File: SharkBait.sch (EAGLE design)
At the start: 12 parts

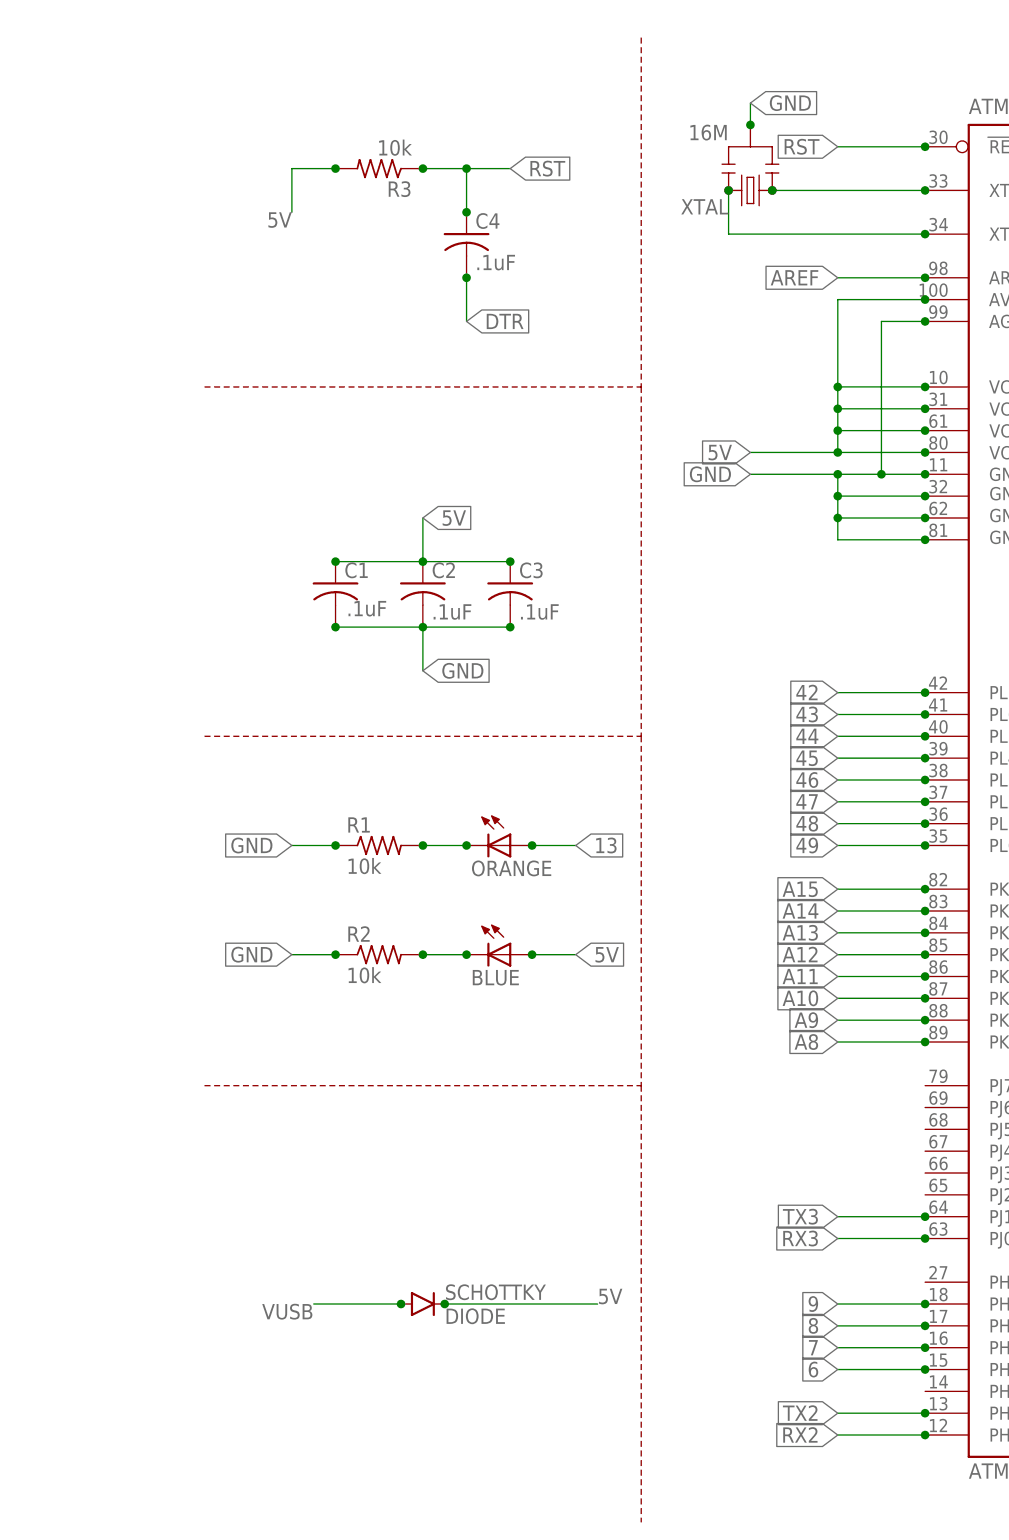
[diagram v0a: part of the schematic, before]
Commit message: menambahkan pin uploader
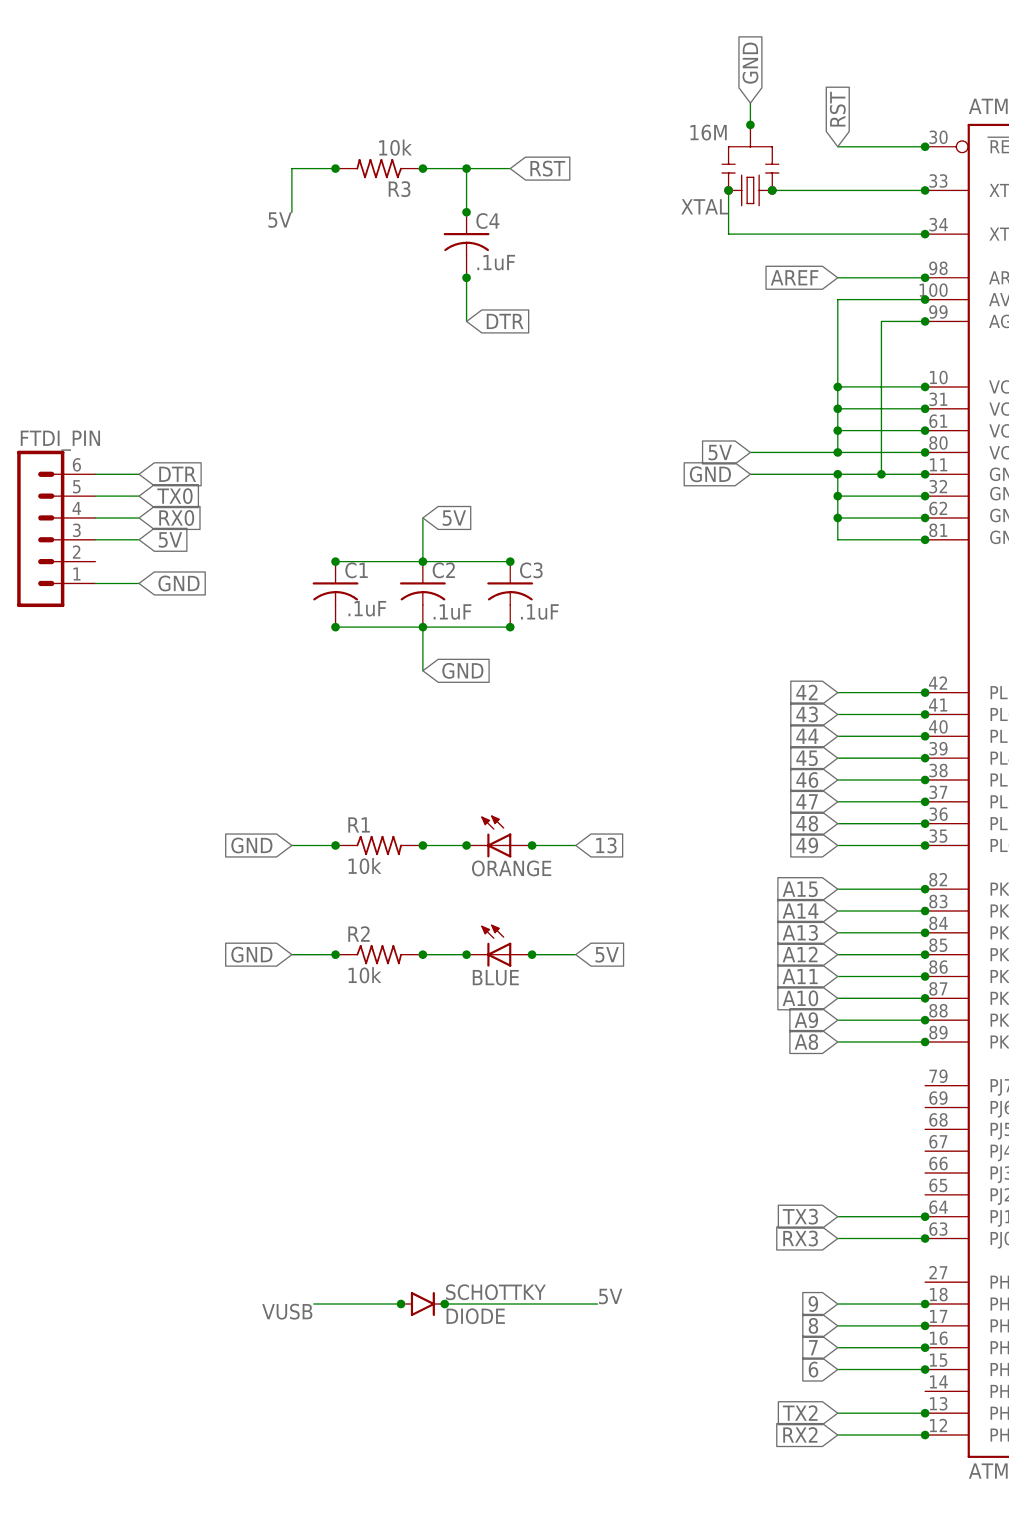
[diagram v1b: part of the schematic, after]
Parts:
- added FTDI_PIN: (no value), con-lstb:MA06-1
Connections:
- net 5V: now also FTDI_PIN.3
- net DTR: now also FTDI_PIN.6
- net GND: now also FTDI_PIN.1
- net RX0: now also FTDI_PIN.4
- net TX0: now also FTDI_PIN.5
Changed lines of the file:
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@@
 <part name="C4" library="Fuzzy" deviceset="CAPACITOR-SMD-0805" device="" value=".1uF"/>
 <part name="SCHOTTKY" library="Fuzzy" deviceset="DIODE" device="" value="DIODE"/>
+<part name="FTDI_PIN" library="con-lstb" deviceset="MA06-1" device=""/>
 </parts>
 <sheets>
 <sheet>
 <plain>
-<wire x1="-99.06" y1="162.56" x2="-99.06" y2="121.92" width="0.1" layer="94" style="longdash"/>
-<wire x1="-99.06" y1="121.92" x2="-99.06" y2="81.28" width="0.1" layer="94" style="longdash"/>
-<wire x1="-99.06" y1="81.28" x2="-99.06" y2="40.64" width="0.1" layer="94" style="longdash"/>
-<wire x1="-99.06" y1="40.64" x2="-99.06" y2="-10.16" width="0.1" layer="94" style="longdash"/>
-<wire x1="-149.86" y1="121.92" x2="-99.06" y2="121.92" width="0.1" layer="94" style="longdash"/>
-<wire x1="-149.86" y1="81.28" x2="-99.06" y2="81.28" width="0.1" layer="94" style="longdash"/>
-<wire x1="-149.86" y1="40.64" x2="-99.06" y2="40.64" width="0.1" layer="94" style="longdash"/>
 <text x="-137.16" y="76.2" size="2" layer="98" ratio="15">Indicator LED's</text>
 <text x="-137.16" y="116.84" size="2" layer="98" ratio="15">Bypass Capacitors</text>
@@
 <instance part="C4" gate="G$1" x="-119.38" y="139.7"/>
 <instance part="SCHOTTKY" gate="G$1" x="-124.46" y="15.24"/>
+<instance part="FTDI_PIN" gate="1" x="-170.18" y="106.68"/>
 </instances>
 <busses>
@@
 <junction x="-121.92" y="15.24"/>
 <wire x1="-121.92" y1="15.24" x2="-104.14" y2="15.24" width="0.1524" layer="91"/>
+</segment>
+<segment>
+<pinref part="FTDI_PIN" gate="1" pin="3"/>
+<wire x1="-162.56" y1="104.14" x2="-157.48" y2="104.14" width="0.1524" layer="91"/>
+<label x="-157.48" y="104.14" size="1.778" layer="95" xref="yes"/>
 </segment>
 </net>
@@
 <pinref part="XTAL" gate="G$1" pin="2"/>
 <wire x1="-86.36" y1="152.4" x2="-86.36" y2="154.94" width="0.1524" layer="91"/>
-<label x="-86.36" y="154.94" size="1.778" layer="95" xref="yes"/>
+<label x="-86.36" y="154.94" size="1.778" layer="95" rot="R90" xref="yes"/>
 <junction x="-86.36" y="152.4"/>
 </segment>
@@
 <junction x="-134.62" y="55.88"/>
 </segment>
+<segment>
+<pinref part="FTDI_PIN" gate="1" pin="1"/>
+<wire x1="-162.56" y1="99.06" x2="-157.48" y2="99.06" width="0.1524" layer="91"/>
+<label x="-157.48" y="99.06" size="1.778" layer="95" xref="yes"/>
+</segment>
 </net>
 <net name="RST" class="0">
@@
 <pinref part="ATMEGA2560" gate="G$1" pin="RESET"/>
 <wire x1="-66.04" y1="149.86" x2="-76.2" y2="149.86" width="0.1524" layer="91"/>
-<label x="-76.2" y="149.86" size="1.778" layer="95" rot="R180" xref="yes"/>
+<label x="-76.2" y="149.86" size="1.778" layer="95" rot="R90" xref="yes"/>
 <junction x="-66.04" y="149.86"/>
 </segment>
@@
 <junction x="-119.38" y="134.62"/>
 </segment>
+<segment>
+<pinref part="FTDI_PIN" gate="1" pin="6"/>
+<wire x1="-162.56" y1="111.76" x2="-157.48" y2="111.76" width="0.1524" layer="91"/>
+<label x="-157.48" y="111.76" size="1.778" layer="95" xref="yes"/>
+</segment>
 </net>
 <net name="N$82" class="0">
@@
 <junction x="5.08" y="40.64"/>
 </segment>
+<segment>
+<pinref part="FTDI_PIN" gate="1" pin="4"/>
+<wire x1="-162.56" y1="106.68" x2="-157.48" y2="106.68" width="0.1524" layer="91"/>
+<label x="-157.48" y="106.68" size="1.778" layer="95" xref="yes"/>
+</segment>
 </net>
 <net name="TX0" class="0">
@@
 <junction x="5.08" y="43.18"/>
 </segment>
-</net>
+<segment>
+<pinref part="FTDI_PIN" gate="1" pin="5"/>
+<wire x1="-162.56" y1="109.22" x2="-157.48" y2="109.22" width="0.1524" layer="91"/>
+<label x="-157.48" y="109.22" size="1.778" layer="95" xref="yes"/>
+</segment>
+</net>

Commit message: Revisi final
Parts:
- removed FTDI_PIN: (no value), con-lstb:MA06-1
- added C11: 100uF, rcl:CPOL-USD
- added C5, C7: 100 uF, rc-master-smd:C_0805
- added C6: 100nF, rcl:C-USC1206
- added C9: 10uF, Fuzzy:CAPACITOR-SMD-0805
- added HT733: HT7333, C_HT7333_SOT89:HT7333
- added J1: BC501SM-TR, C_BC501SM-TR:BC501SM-TR
- added Q1: L78M05CDT, C_L78M05CDT:L78M05CDT
- added R10, R11, R4, R8: 1K8, rc-master-smd:R_0805
- added R12, R13, R7, R9: 3K3, rc-master-smd:R_0805
- added R5, R6: (no value), rc-master-smd:R_0805
- added U$1: WEMOS_SD_D1_MINI, C_WEMOS_SD_D1_MINI:WEMOS_SD_D1_MINI
- added U$2: SIM7000, C_SIM7000:SIM7000
- added U$3: JST-PH_5-PIN_HEADER, srg:JST-PH_5-PIN_HEADER
- added U$4: JST-PH_2-PIN_HEADER, srg:JST-PH_2-PIN_HEADER
- added U$5: JST-PH_3-PIN_HEADER, srg:JST-PH_3-PIN_HEADER
- added U$6: JST-PH_4-PIN_HEADER, srg:JST-PH_4-PIN_HEADER
- added U2: DS3231M+, C_DS3231M_:DS3231M+
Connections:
- removed net 10: ATMEGA2560.(OC2A/PCINT4)PB4
- removed net 11: ATMEGA2560.(OC1A/PCINT5)PB5
- removed net 12: ATMEGA2560.(OC1B/PCINT6)PB6
- removed net 2: ATMEGA2560.(OC3B/INT4)PE4
- removed net 20: ATMEGA2560.(SDA/INT1)PD1
- removed net 21: ATMEGA2560.(SCL/INT0)PD0
- removed net 22: ATMEGA2560.(AD0)PA0
- removed net 23: ATMEGA2560.(AD1)PA1
- removed net 24: ATMEGA2560.(AD2)PA2
- removed net 25: ATMEGA2560.(AD3)PA3
- removed net 26: ATMEGA2560.(AD4)PA4
- removed net 27: ATMEGA2560.(AD5)PA5
- removed net 28: ATMEGA2560.(AD6)PA6
- removed net 29: ATMEGA2560.(AD7)PA7
- removed net 3: ATMEGA2560.(OC3C/INT5)PE5
- removed net 30: ATMEGA2560.(A15)PC7
- removed net 31: ATMEGA2560.(A14)PC6
- removed net 32: ATMEGA2560.(A13)PC5
- removed net 33: ATMEGA2560.(A12)PC4
- removed net 34: ATMEGA2560.(A11)PC3
- removed net 35: ATMEGA2560.(A10)PC2
- removed net 36: ATMEGA2560.(A9)PC1
- removed net 37: ATMEGA2560.(A8)PC0
- removed net 38: ATMEGA2560.(T0)PD7
- removed net 39: ATMEGA2560.(ALE)PG2
- removed net 4: ATMEGA2560.(OC0B)PG5
- removed net 40: ATMEGA2560.(RD)PG1
- removed net 41: ATMEGA2560.(WR)PG0
- removed net 42: ATMEGA2560.PL7
- removed net 43: ATMEGA2560.PL6
- removed net 44: ATMEGA2560.PL5(OC5C)
- removed net 45: ATMEGA2560.PL4(OC5B)
- removed net 46: ATMEGA2560.PL3(OC5A)
- removed net 47: ATMEGA2560.PL2(T5)
- removed net 48: ATMEGA2560.PL1(ICP5)
- removed net 49: ATMEGA2560.PL0(ICP4)
- removed net 5: ATMEGA2560.(OC3A/AIN1)PE3
- removed net 50: ATMEGA2560.(MISO/PCINT3)PB3
- removed net 51: ATMEGA2560.(MOSI/PCINT2)PB2
- removed net 52: ATMEGA2560.(SCK/PCINT1)PB1
- removed net 53: ATMEGA2560.(SS/PCINT0)PB0
- removed net 6: ATMEGA2560.PH3(OC4A)
- removed net 7: ATMEGA2560.PH4(OC4B)
- removed net 8: ATMEGA2560.PH5(OC4C)
- removed net 9: ATMEGA2560.PH6(OC2B)
- removed net A10: ATMEGA2560.PK2(ADC10/PCINT18)
- removed net A11: ATMEGA2560.PK3(ADC11/PCINT19)
- removed net A12: ATMEGA2560.PK4(ADC12/PCINT20)
- removed net A13: ATMEGA2560.PK5(ADC13/PCINT21)
- removed net A14: ATMEGA2560.PK6(ADC14/PCINT22)
- removed net A15: ATMEGA2560.PK7(ADC15/PCINT23)
- removed net A2: ATMEGA2560.(ADC2)PF2
- removed net A3: ATMEGA2560.(ADC3)PF3
- removed net A4: ATMEGA2560.(ADC4/TCK)PF4
- removed net A5: ATMEGA2560.(ADC5/TMS)PF5
- removed net A6: ATMEGA2560.(ADC6/TDO)PF6
- removed net A7: ATMEGA2560.(ADC7/TDI)PF7
- removed net A8: ATMEGA2560.PK0(ADC8/PCINT16)
- removed net A9: ATMEGA2560.PK1(ADC9/PCINT17)
- removed net RX2: ATMEGA2560.PH0(RXD2)
- removed net RX3: ATMEGA2560.PJ0(RXD3/PCINT9)
- removed net TX2: ATMEGA2560.PH1(TXD2)
- removed net TX3: ATMEGA2560.PJ1(TXD3/PCINT10)
- removed net VUSB: SCHOTTKY.A
- new net 3V3: C7.2, C9.1, HT733.VOUT, R5.1, R6.2, U$1.3V3, U2.VCC
- new net D13: ATMEGA2560.(OC0A/OC1C/PCINT7)PB7
- new net D3: ATMEGA2560.(OC3C/INT5)PE5, U2.!INT/SQW
- new net D4: ATMEGA2560.(OC0B)PG5, ATMEGA2560.(OC3B/INT4)PE4, U$5.1
- new net D5: ATMEGA2560.(OC3A/AIN1)PE3, U$2.KEY
- new net D6: ATMEGA2560.PH3(OC4A), U$2.SL
- new net D7: ATMEGA2560.PH4(OC4B), U$6.2
- new net MISO: ATMEGA2560.(MISO/PCINT3)PB3, R10.1, R10.2, R13.2, U$1.MOSI
- new net MOSI: ATMEGA2560.(MOSI/PCINT2)PB2, R4.1
- new net N$1: J1.POS, U2.VBAT
- new net N$2: R4.2, R7.2, U$1.MISO
- new net SCK: ATMEGA2560.(SCK/PCINT1)PB1, R11.1, R11.2, R12.2, U$1.CLK
- new net SCK1: R8.2, R9.2, U$1.CS
- new net SCL: ATMEGA2560.(SCL/INT0)PD0, R6.1, U2.SCL
- new net SDA: ATMEGA2560.(SDA/INT1)PD1, R5.2, U2.SDA
- new net SS: ATMEGA2560.(SS/PCINT0)PB0, R8.1
- new net VBAT: C5.2, C6.1, HT733.VIN, Q1.IN, U$4.1
- new net VCC: SCHOTTKY.A, U$3.4
- net 13: no longer ATMEGA2560.(OC0A/OC1C/PCINT7)PB7
- net 5V: now also C11.+, Q1.OUT, U$2.V, U$6.1; no longer FTDI_PIN.3
- net A0: now also U$6.3
- net A1: now also U$5.2
- net DTR: now also U$3.1; no longer FTDI_PIN.6
- net GND: now also C11.-, C5.1, C6.2, C7.1, C9.2, HT733.GND, J1.NEG, Q1.GND, R12.1, R13.1, R7.1, R9.1, U$2.GND, U$2.GND1, U$3.5, U$4.2, U$5.3, U$6.4, U2.GND; no longer FTDI_PIN.1
- net RX0: now also U$3.3; no longer FTDI_PIN.4
- net RX1: now also U$2.TX
- net TX0: now also U$3.2; no longer FTDI_PIN.5
- net TX1: now also U$2.RX
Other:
- note added: "REGULATOR HT7333"
- note added: "REGULATOR LM78M05"
- note added: "RTC DS3231"
- note added: "SD CARD MODUL"
- note added: "SD Card Modul"
- note added: "Uploader"
- moved on the sheet: ATMEGA2560, BLUE, C1, C2, C3, C4, ORANGE, R1, R2, R3, SCHOTTKY, XTAL

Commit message: revisi 3, termasuk pembetulan pin yang terbalik, dan regulator 5v yang terbalik
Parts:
- removed SCHOTTKY: DIODE, Fuzzy:DIODE
- removed U$4: JST-PH_2-PIN_HEADER, srg:JST-PH_2-PIN_HEADER
- added BAT: JST-PH_2-PIN_HEADER, srg:JST-PH_2-PIN_HEADER
- renumbered U$3 to FTDI, U$5 to SENSOR0, U$6 to SENSOR1
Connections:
- removed net 13: ORANGE.A
- removed net N$2: R4.2, R7.2, U$1.MISO
- removed net VCC: FTDI.4, SCHOTTKY.A
- new net N$3: R4.2, R7.2, U$1.MOSI
- net 5V: now also FTDI.4; no longer SCHOTTKY.C
- net D13: now also ORANGE.A
- net GND: now also BAT.1; no longer U$4.2
- net MISO: now also U$1.MISO; no longer U$1.MOSI
- net VBAT: now also BAT.2; no longer U$4.1
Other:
- note added: "3"
- moved on the sheet: C11, Q1
